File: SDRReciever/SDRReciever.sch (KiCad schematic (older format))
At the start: 78 parts, among them J1 Conn_Coaxial, J10 I_0, J11 I_180, J12 Q_90, J13 Q_270, J14 I_OUT, J15 Q_OUT, J16 5V, J17 4.3V, J18 Conn_01x02_Female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

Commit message: Added potentiometer, voltage buffer, clk gen pull up resistors, comments, and corrected gain resistors to 1k
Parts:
- removed R7, R8: 10k, Resistor_THT:R_Axial_DIN0207_L6.3mm_D2.5mm_P7.62mm_Horizontal, symbol Device:R
- added R? (x2): 1k, symbol Device:R
- added RV?: 100k, symbol Device:R_POT
- added U?: LM741, symbol Amplifier_Operational:LM741
- J5: value CLK_2 -> CLK_1
- J6: value CLK_3 -> CLK_2
- J7: value CLK_1 -> CLK_0
- R3, R4: value 33 -> 1k
- Y1: value Crystal -> ATS250
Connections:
- net +3V3: now also R?.1, R?.1
- net +4.3V: now also RV?.1; no longer C24.2
- net +5V: now also U?.7 (V+)
- net FIL_OUT: now also RV?.2
- net GND: now also RV?.3, U?.4 (V-)
- net GNDA: now also U?.2 (-), U?.6; no longer R17.1, R2.2
- net SCL: now also R?.2
- net SDA: now also R?.2
- new net: C24.2, R17.1, R2.2, U?.3 (+)
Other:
- note added: "25MHz"
- note added: "The INA821ID Amps require the REF\ninput to have a voltage source with a\nlow output impedence. The LM741\nvoltage buffer handles this"
- note added: "Tunable\n2.15V Bias"
- note added: "Two-Pole Low Pass Filter\nUsing 2-Channel Op Amp\n100kHz Cutoff"
- note added: "With 5-10MHz, CLK_0 will \nbe around 20 - 40 MHz"
- note removed: "2.15V Bias"
- note removed: "Confirm no pull ups are fine\nfor the SCL SDA lines"
- note removed: "Duty cycle of Tayloe Mixer\nmakes the input impedence\n1/4, making Gain = R1/(4*R3)\n10 Ohms added for current control"
- note removed: "Two-Pole Low Pass Filter\nUsing 2-Channel Op Amp"
- note removed: "With 5-10MHz, LO will be\naround 20 - 40 MHz"
- moved on the sheet: C11, C24, C9, J16, J17, JP3, Q1, R1, R17, R2

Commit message: Changed PCB silkscreen title block, renamed some image files to be more specific to the revision they refer to, added SVGs for clearer documentation imagery
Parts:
- gave numbers to parts that had none: 4
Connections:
- no-connect marks 25 -> 27
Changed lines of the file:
@@
 	3450 4850 3650 4850
 $Comp
-L Amplifier_Operational:LM741 U?
+L Amplifier_Operational:LM741 U7
 U 1 1 5EDAB873
 P 9825 5625
-F 0 "U?" H 10169 5671 50  0000 L CNN
+F 0 "U7" H 10169 5671 50  0000 L CNN
 F 1 "LM741" H 10169 5580 50  0000 L CNN
 F 2 "" H 9875 5675 50  0001 C CNN
@@
 $EndComp
 $Comp
-L power:+5V #PWR?
+L power:+5V #PWR042
 U 1 1 5EDC9E45
 P 9725 5325
-F 0 "#PWR?" H 9725 5175 50  0001 C CNN
+F 0 "#PWR042" H 9725 5175 50  0001 C CNN
 F 1 "+5V" H 9875 5375 50  0000 C CNN
 F 2 "" H 9725 5325 50  0001 C CNN
@@
 	10125 6175 10125 5625
 $Comp
-L power:GND #PWR?
+L power:GND #PWR026
 U 1 1 5EDF4DF4
 P 8925 6100
-F 0 "#PWR?" H 8925 5850 50  0001 C CNN
+F 0 "#PWR026" H 8925 5850 50  0001 C CNN
 F 1 "GND" H 9075 6050 50  0000 C CNN
 F 2 "" H 8925 6100 50  0001 C CNN
@@
 The INA821ID Amps require the REF\ninput to have a voltage source with a\nlow output impedence. The LM741\nvoltage buffer handles this
 $Comp
-L Device:R_POT RV?
+L Device:R_POT RV1
 U 1 1 5EE830FE
 P 5450 1200
-F 0 "RV?" V 5243 1200 50  0000 C CNN
+F 0 "RV1" V 5243 1200 50  0000 C CNN
 F 1 "100k" V 5334 1200 50  0000 C CNN
 F 2 "" H 5450 1200 50  0001 C CNN
@@
 	700  7525 1075 7525
 $Comp
-L Device:R R?
+L Device:R R7
 U 1 1 5EF8A4E5
 P 825 7225
-F 0 "R?" H 895 7271 50  0000 L CNN
+F 0 "R7" H 895 7271 50  0000 L CNN
 F 1 "1k" H 895 7180 50  0000 L CNN
 F 2 "" V 755 7225 50  0001 C CNN
@@
 $EndComp
 $Comp
-L Device:R R?
+L Device:R R8
 U 1 1 5EF8B556
 P 1075 7225
-F 0 "R?" H 1145 7271 50  0000 L CNN
+F 0 "R8" H 1145 7271 50  0000 L CNN
 F 1 "1k" H 1145 7180 50  0000 L CNN
 F 2 "" V 1005 7225 50  0001 C CNN
@@
 	1075 7525 1075 7375
 $Comp
-L power:+3.3V #PWR?
+L power:+3.3V #PWR025
 U 1 1 5EFAA0AC
 P 650 7075
-F 0 "#PWR?" H 650 6925 50  0001 C CNN
+F 0 "#PWR025" H 650 6925 50  0001 C CNN
 F 1 "+3.3V" H 650 7225 50  0000 C CNN
 F 2 "" H 650 7075 50  0001 C CNN
@@
 Text Notes 750  6725 0    50   ~ 0
 25MHz
+NoConn ~ 9825 5925
+NoConn ~ 9925 5925
 $EndSCHEMATC

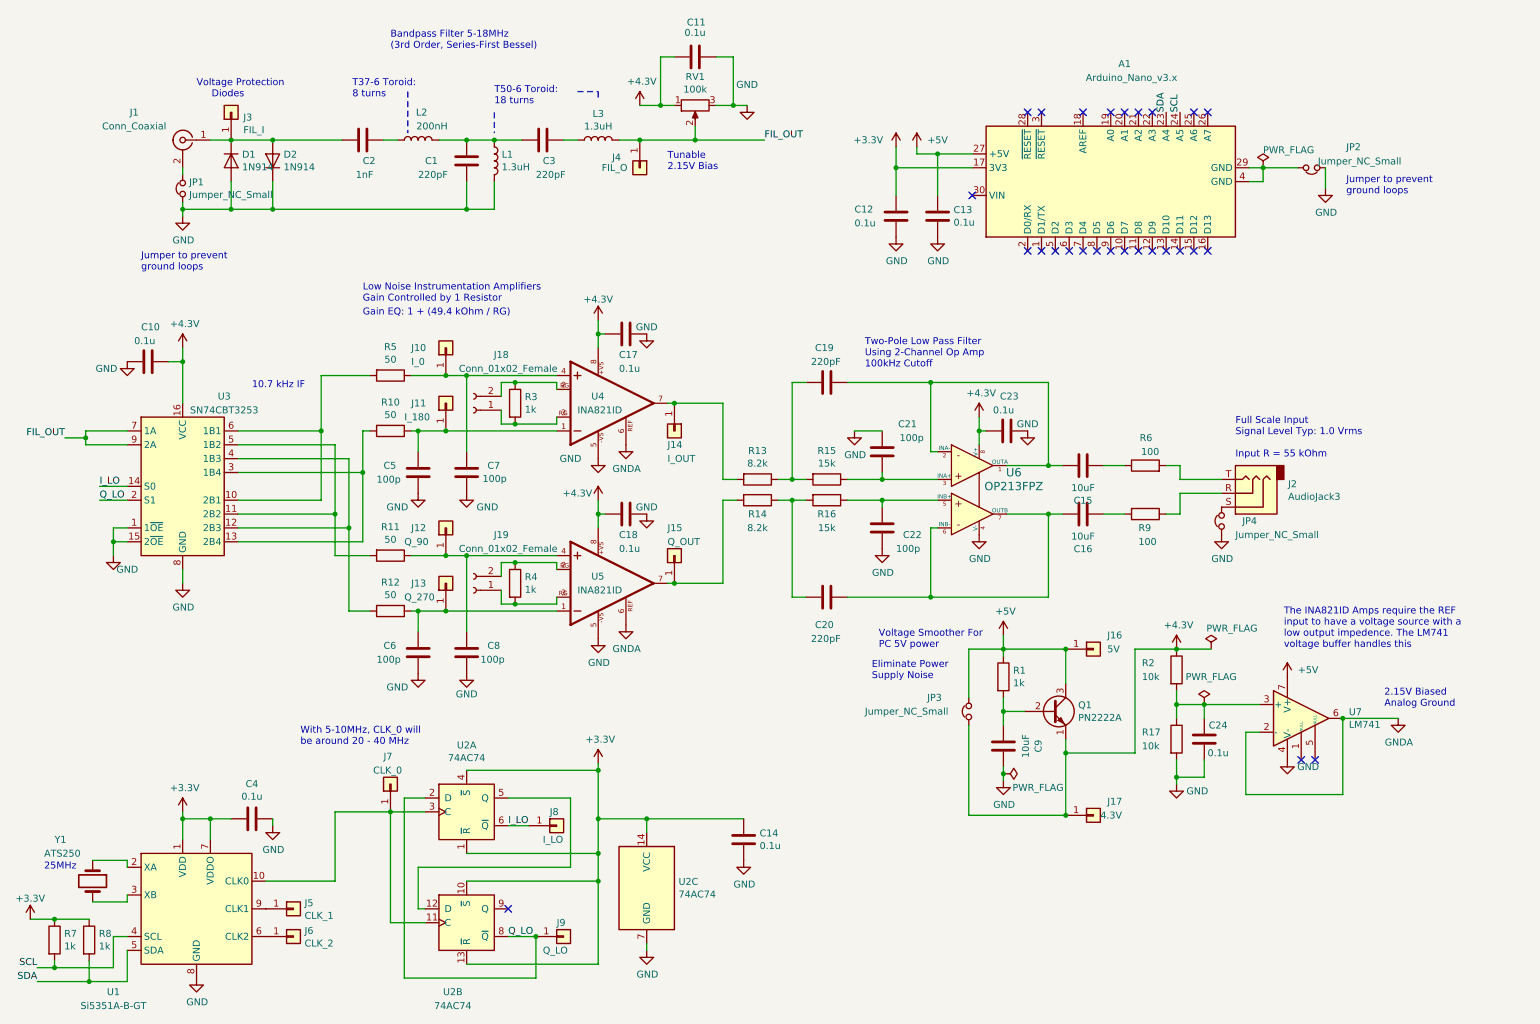
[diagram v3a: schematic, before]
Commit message: Added notes to schematic and more images
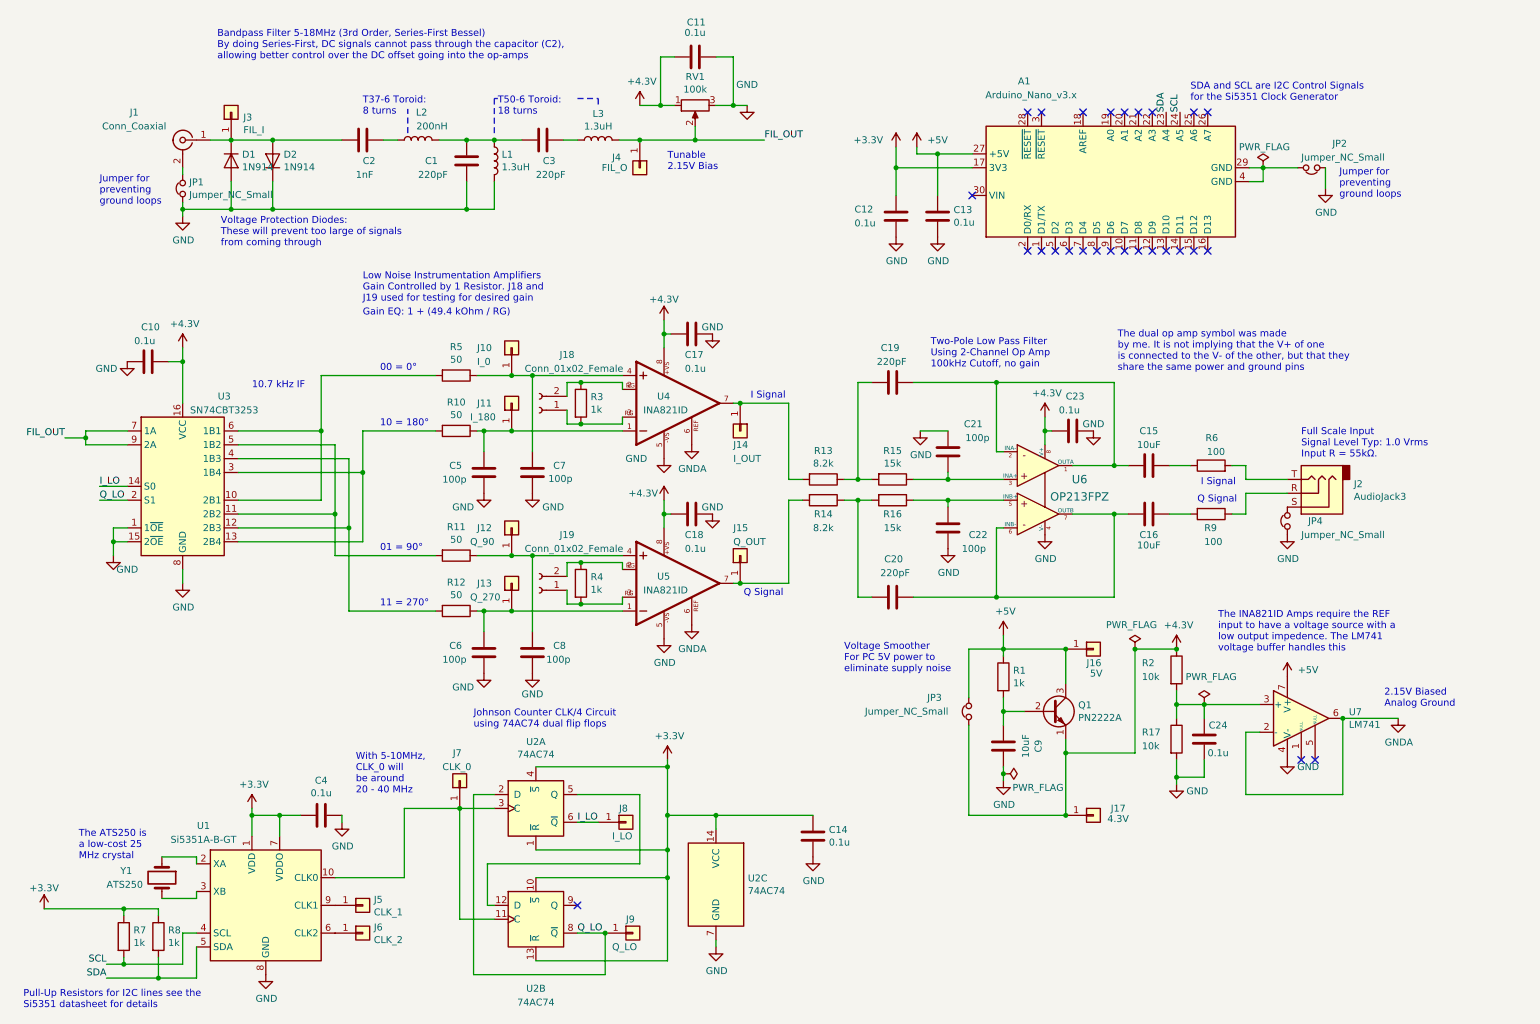
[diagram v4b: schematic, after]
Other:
- note added: "00 = 0°"
- note added: "01 = 90°"
- note added: "10 = 180°"
- note added: "11 = 270°"
- note added: "Bandpass Filter 5-18MHz (3rd Order, Series-First Bessel)\nBy doing Series-First, DC signals cannot pass through the capacitor (C2), \nallowing better control over the DC offset going into the op-amps"
- note added: "Full Scale Input \nSignal Level Typ: 1.0 Vrms\nInput R = 55kΩ."
- note added: "I Signal"
- note added: "Johnson Counter CLK/4 Circuit\nusing 74AC74 dual flip flops"
- note added: "Jumper for\npreventing \nground loops"
- note added: "Low Noise Instrumentation Amplifiers\nGain Controlled by 1 Resistor. J18 and \nJ19 used for testing for desired gain"
- note added: "Pull-Up Resistors for I2C lines see the \nSi5351 datasheet for details"
- note added: "Q Signal"
- note added: "SDA and SCL are I2C Control Signals \nfor the Si5351 Clock Generator"
- note added: "The ATS250 is \na low-cost 25 \nMHz crystal"
- note added: "The dual op amp symbol was made\nby me. It is not implying that the V+ of one\nis connected to the V- of the other, but that they\nshare the same power and ground pins"
- note added: "Two-Pole Low Pass Filter\nUsing 2-Channel Op Amp\n100kHz Cutoff, no gain"
- note added: "Voltage Protection Diodes:\nThese will prevent too large of signals \nfrom coming through"
- note added: "Voltage Smoother \nFor PC 5V power to \neliminate supply noise"
- note added: "With 5-10MHz, \nCLK_0 will \nbe around \n20 - 40 MHz"
- note removed: "25MHz"
- note removed: "Bandpass Filter 5-18MHz\n(3rd Order, Series-First Bessel)"
- note removed: "Eliminate Power\nSupply Noise"
- note removed: "Full Scale Input \nSignal Level Typ: 1.0 Vrms\n\nInput R = 55 kOhm"
- note removed: "Jumper to prevent \nground loops"
- note removed: "Low Noise Instrumentation Amplifiers\nGain Controlled by 1 Resistor"
- note removed: "Two-Pole Low Pass Filter\nUsing 2-Channel Op Amp\n100kHz Cutoff"
- note removed: "Voltage Protection \n Diodes"
- note removed: "Voltage Smoother For\nPC 5V power"
- note removed: "With 5-10MHz, CLK_0 will \nbe around 20 - 40 MHz"
- moved on the sheet: C14, C15, C16, C17, C18, C19, C20, C21, C22, C23, C4, C5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

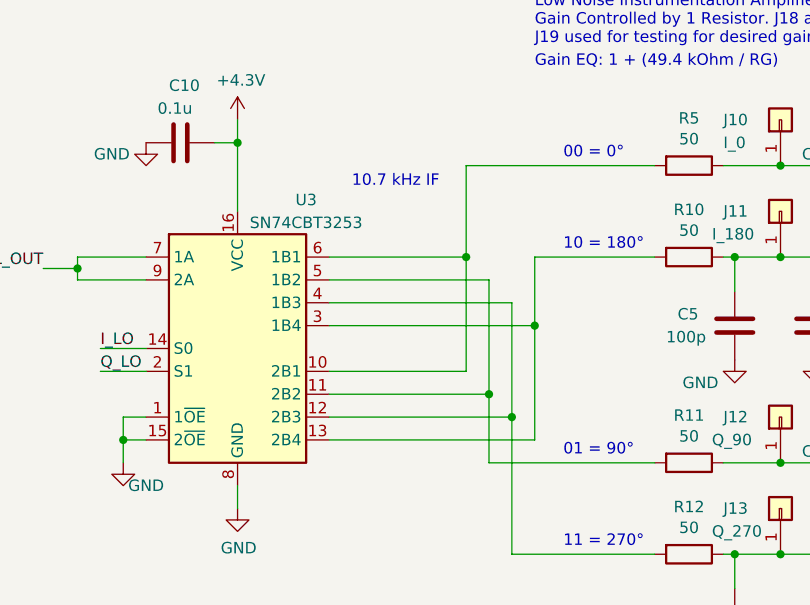
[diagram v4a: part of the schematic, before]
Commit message: Added issue4 testing images
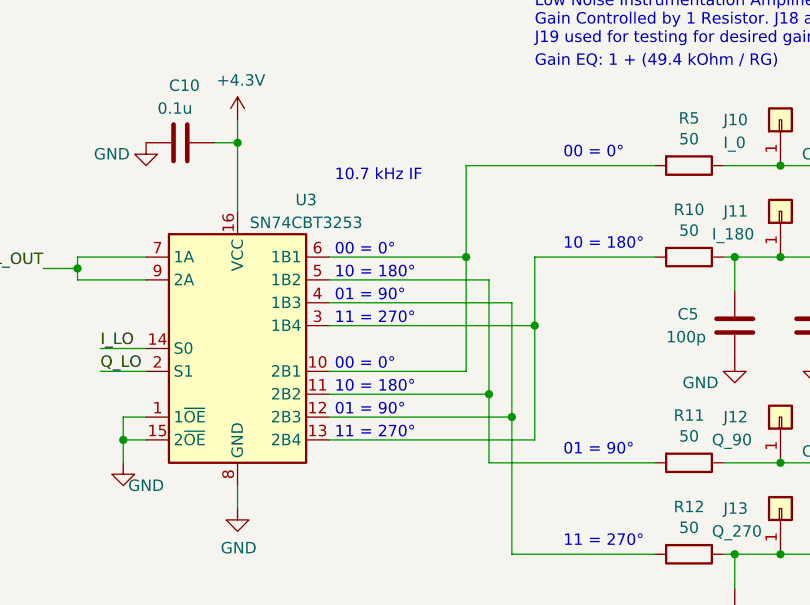
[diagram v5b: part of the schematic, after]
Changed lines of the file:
@@
 Wire Wire Line
 	1850 6925 1850 6875
-Text Notes 2250 3250 0    50   ~ 0
+Text Notes 2175 3225 0    50   ~ 0
 10.7 kHz IF
-Text Notes 2000 875  0    50   ~ 0
-Bandpass Filter 5-18MHz (3rd Order, Series-First Bessel)\nBy doing Series-First, DC signals cannot pass through the capacitor (C2), \nallowing better control over the DC offset going into the op-amps
-Text Notes 2025 2225 0    50   ~ 0
-Voltage Protection Diodes:\nThese will prevent too large of signals \nfrom coming through
 $Comp
 L power:GND #PWR015
@@
 Wire Notes Line
 	3375 1400 3375 1225
-Text Notes 1150 1925 0    50   ~ 0
-Jumper for\npreventing \nground loops
 Wire Notes Line
 	4600 1150 4750 1150
@@
 Text Notes 3175 4825 0    50   ~ 0
 11 = 270°
+Text Notes 1150 1925 0    50   ~ 0
+Jumper for\npreventing \nground loops
+Text Notes 2000 875  0    50   ~ 0
+Bandpass Filter 5-18MHz (3rd Order, Series-First Bessel)\nBy doing Series-First, DC signals cannot pass through the capacitor (C2), \nallowing better control over the DC offset going into the op-amps
+Text Notes 2025 2225 0    50   ~ 0
+Voltage Protection Diodes:\nThese will prevent too large of signals \nfrom coming through
+Text Notes 2175 3550 0    50   ~ 0
+00 = 0°
+Text Notes 2175 4050 0    50   ~ 0
+00 = 0°
+Text Notes 2175 3650 0    50   ~ 0
+10 = 180°
+Text Notes 2175 4150 0    50   ~ 0
+10 = 180°
+Text Notes 2175 3750 0    50   ~ 0
+01 = 90°
+Text Notes 2175 4250 0    50   ~ 0
+01 = 90°
+Text Notes 2175 4350 0    50   ~ 0
+11 = 270°
+Text Notes 2175 3850 0    50   ~ 0
+11 = 270°
 $EndSCHEMATC
